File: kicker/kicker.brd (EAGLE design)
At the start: 59.7 x 56.3 mm, 26 parts, among them T1 NPN_BC817,215, T3 NPN_BC817,215, X1 JST-XH-06-PIN-LONG-PAD

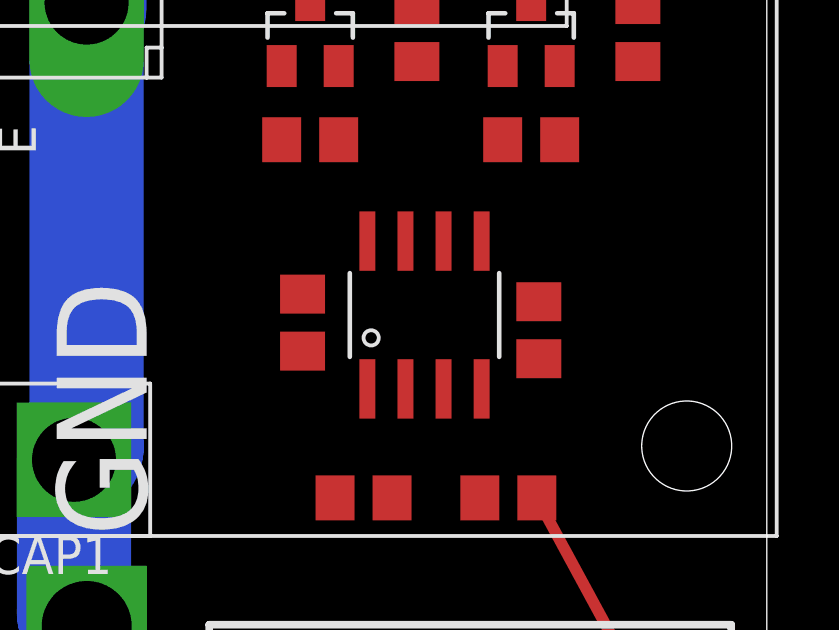
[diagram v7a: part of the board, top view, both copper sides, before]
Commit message: Adding optional npn for kicking
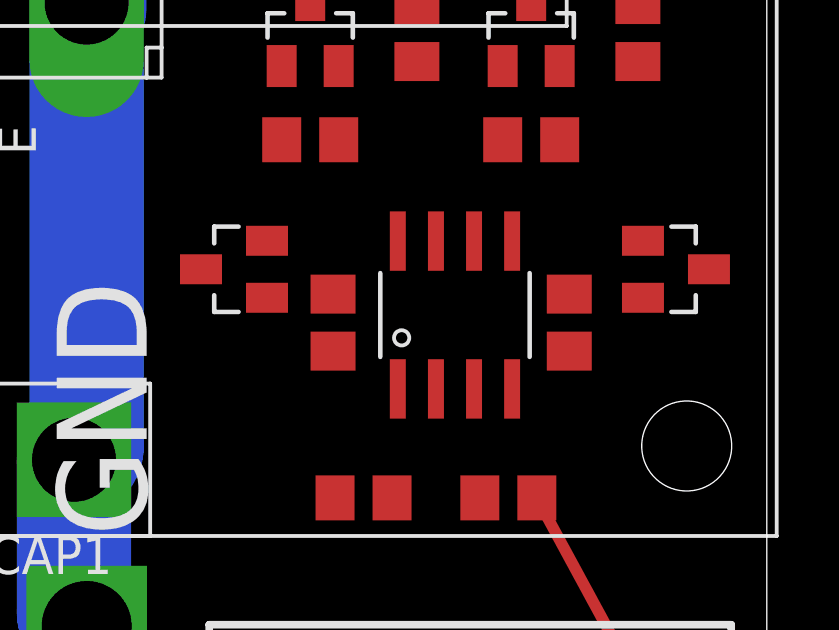
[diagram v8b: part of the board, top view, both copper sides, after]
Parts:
- added T2, T4: NPN_BC817,215, rhoban:SOT-23
- moved R8 1.05 mm to (53.1, 14.7)
- moved R7 1.02 mm to (45.2, 14.7)
- moved U$4 1.02 mm to (49.3, 15.0)
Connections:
- removed net N$10: R8.1, U$4.3
- removed net N$9: R7.1, U$4.1
- new net KICK1R: R7.1, T2.1, U$4.1
- new net KICK2R: R8.1, T4.1, U$4.3
- net GND: now also T2.2, T4.2
- net KICK_TR1: now also T2.3
- net KICK_TR2: now also T4.3
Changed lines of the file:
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@@
 <param name="mtCopper" value="0.035mm 0.035mm 0.035mm 0.035mm 0.035mm 0.035mm 0.035mm 0.035mm 0.035mm 0.035mm 0.035mm 0.035mm 0.035mm 0.035mm 0.035mm 0.035mm"/>
 <param name="mtIsolate" value="1.5mm 0.15mm 0.2mm 0.15mm 0.2mm 0.15mm 0.2mm 0.15mm 0.2mm 0.15mm 0.2mm 0.15mm 0.2mm 0.15mm 0.2mm"/>
-<param name="mdWireWire" value="10mil"/>
+<param name="mdWireWire" value="15mil"/>
 <param name="mdWirePad" value="20mil"/>
 <param name="mdWireVia" value="20mil"/>
@@
 <attribute name="FARNELL" value="2446965" x="51.816" y="28.702" size="1.778" layer="27" rot="R270" display="off"/>
 </element>
-<element name="U$4" library="rhoban" package="SO8" value="ACPL-227-500E" x="48.26" y="14.986" rot="R90">
-<attribute name="FARNELL" value="1634749RL" x="48.26" y="14.986" size="1.778" layer="27" rot="R90" display="off"/>
-</element>
-<element name="R7" library="rhoban" package="R0805" value="3K" x="44.196" y="14.732" rot="R90">
-<attribute name="FARNELL" value="2446965" x="44.196" y="14.732" size="1.778" layer="27" rot="R90" display="off"/>
-</element>
-<element name="R8" library="rhoban" package="R0805" value="3K" x="52.07" y="14.478" rot="R90">
-<attribute name="FARNELL" value="2446965" x="52.07" y="14.478" size="1.778" layer="27" rot="R90" display="off"/>
+<element name="U$4" library="rhoban" package="SO8" value="ACPL-227-500E" x="49.276" y="14.986" rot="R90">
+<attribute name="FARNELL" value="1634749RL" x="49.276" y="14.986" size="1.778" layer="27" rot="R90" display="off"/>
+</element>
+<element name="R7" library="rhoban" package="R0805" value="3K" x="45.212" y="14.732" rot="R90">
+<attribute name="FARNELL" value="2446965" x="45.212" y="14.732" size="1.778" layer="27" rot="R90" display="off"/>
+</element>
+<element name="R8" library="rhoban" package="R0805" value="3K" x="53.086" y="14.732" rot="R90">
+<attribute name="FARNELL" value="2446965" x="53.086" y="14.732" size="1.778" layer="27" rot="R90" display="off"/>
+</element>
+<element name="T2" library="rhoban" package="SOT-23" value="NPN_BC817,215" x="41.91" y="16.51" rot="R90">
+<attribute name="FARNELL" value="1081223" x="41.91" y="16.51" size="1.778" layer="27" rot="R90" display="off"/>
+</element>
+<element name="T4" library="rhoban" package="SOT-23" value="NPN_BC817,215" x="56.642" y="16.51" rot="R270">
+<attribute name="FARNELL" value="1081223" x="57.15" y="16.51" size="1.778" layer="27" rot="R270" display="off"/>
 </element>
 </elements>
@@
 <contactref element="X1" pad="5"/>
 <contactref element="R8" pad="2"/>
-<wire x1="52.07" y1="15.428" x2="53.594" y2="1.27" width="0" layer="19" extent="1-1"/>
+<wire x1="53.594" y1="1.27" x2="53.086" y2="15.682" width="0" layer="19" extent="1-1"/>
 </signal>
 <signal name="GND" class="2">
@@
 <contactref element="U$4" pad="7"/>
 <contactref element="U$4" pad="5"/>
-<wire x1="50.165" y1="17.4498" x2="52.766" y2="23.284" width="0" layer="19" extent="1-1"/>
-<wire x1="47.625" y1="17.4498" x2="50.165" y2="17.4498" width="0" layer="19" extent="1-1"/>
-<wire x1="50.165" y1="12.5222" x2="50.165" y2="17.4498" width="0" layer="19" extent="1-1"/>
-<wire x1="47.625" y1="12.5222" x2="50.165" y2="12.5222" width="0" layer="19" extent="1-1"/>
-<wire x1="50.104" y1="8.89" x2="50.165" y2="12.5222" width="0" layer="19" extent="1-1"/>
-<wire x1="45.4" y1="23.284" x2="47.625" y2="17.4498" width="0" layer="19" extent="1-1"/>
-<wire x1="36.996" y1="25.4" x2="45.4" y2="23.284" width="0" layer="19" extent="1-1"/>
+<wire x1="32.766" y1="32.766" x2="37.084" y2="28.448" width="3.81" layer="16" curve="-90"/>
+<wire x1="37.084" y1="28.448" x2="37.084" y2="25.146" width="3.81" layer="16"/>
+<contactref element="T2" pad="2"/>
+<contactref element="T4" pad="2"/>
+<wire x1="51.181" y1="17.4498" x2="52.766" y2="23.284" width="0" layer="19" extent="1-1"/>
+<wire x1="48.641" y1="17.4498" x2="51.181" y2="17.4498" width="0" layer="19" extent="1-1"/>
+<wire x1="55.542" y1="15.56" x2="51.181" y2="17.4498" width="0" layer="19" extent="1-1"/>
+<wire x1="51.181" y1="12.5222" x2="51.181" y2="17.4498" width="0" layer="19" extent="1-1"/>
+<wire x1="48.641" y1="12.5222" x2="51.181" y2="12.5222" width="0" layer="19" extent="1-1"/>
+<wire x1="50.104" y1="8.89" x2="51.181" y2="12.5222" width="0" layer="19" extent="1-1"/>
+<wire x1="43.01" y1="17.46" x2="48.641" y2="12.5222" width="0" layer="19" extent="1-1"/>
+<wire x1="45.4" y1="23.284" x2="48.641" y2="17.4498" width="0" layer="19" extent="1-1"/>
+<wire x1="36.996" y1="10.58" x2="43.01" y2="17.46" width="0" layer="19" extent="1-16"/>
+<wire x1="37.084" y1="25.146" x2="36.996" y2="25.4" width="0" layer="19" extent="16-16"/>
 <wire x1="43.434" y1="1.27" x2="37" y2="0.17" width="0" layer="19" extent="16-16"/>
 <wire x1="8.72" y1="14.92" x2="19.47" y2="25.4" width="0" layer="19" extent="1-1"/>
 <wire x1="11" y1="4.62" x2="8.72" y2="14.92" width="0" layer="19" extent="1-1"/>
-<wire x1="32.766" y1="32.766" x2="37.084" y2="28.448" width="3.81" layer="16" curve="-90"/>
-<wire x1="37.084" y1="28.448" x2="37.084" y2="25.146" width="3.81" layer="16"/>
-<wire x1="37.084" y1="25.146" x2="36.996" y2="25.4" width="0" layer="19" extent="1-16"/>
 </signal>
 <signal name="N$4">
@@
 <contactref element="X1" pad="4"/>
 <contactref element="R7" pad="2"/>
-<wire x1="44.196" y1="15.682" x2="51.054" y2="1.27" width="0" layer="19" extent="1-1"/>
+<wire x1="51.054" y1="1.27" x2="45.212" y2="15.682" width="0" layer="19" extent="1-1"/>
 </signal>
 <signal name="CAP">
@@
 <contactref element="T1" pad="1"/>
 <contactref element="U$4" pad="8"/>
+<contactref element="T2" pad="3"/>
 <wire x1="43.5" y1="20.828" x2="43.5" y2="23.284" width="0" layer="19" extent="1-1"/>
-<wire x1="46.355" y1="17.4498" x2="43.5" y2="20.828" width="0" layer="19" extent="1-1"/>
+<wire x1="40.81" y1="16.51" x2="43.5" y2="20.828" width="0" layer="19" extent="1-1"/>
+<wire x1="47.371" y1="17.4498" x2="43.5" y2="20.828" width="0" layer="19" extent="1-1"/>
 </signal>
 <signal name="KICK_TR2">
@@
 <contactref element="T3" pad="1"/>
 <contactref element="U$4" pad="6"/>
+<contactref element="T4" pad="3"/>
 <wire x1="50.866" y1="20.828" x2="50.866" y2="23.284" width="0" layer="19" extent="1-1"/>
-<wire x1="48.895" y1="17.4498" x2="50.866" y2="20.828" width="0" layer="19" extent="1-1"/>
+<wire x1="49.911" y1="17.4498" x2="50.866" y2="20.828" width="0" layer="19" extent="1-1"/>
+<wire x1="57.742" y1="16.51" x2="49.911" y2="17.4498" width="0" layer="19" extent="1-1"/>
 </signal>
 <signal name="N$7">
@@
 <wire x1="8.47" y1="25.4" x2="51.816" y2="29.652" width="0" layer="19" extent="1-1"/>
 </signal>
-<signal name="N$9">
+<signal name="KICK1R">
 <contactref element="U$4" pad="1"/>
 <contactref element="R7" pad="1"/>
-<wire x1="46.355" y1="12.5222" x2="44.196" y2="13.782" width="0" layer="19" extent="1-1"/>
-</signal>
-<signal name="N$10">
+<contactref element="T2" pad="1"/>
+<wire x1="45.212" y1="13.782" x2="47.371" y2="12.5222" width="0" layer="19" extent="1-1"/>
+<wire x1="43.01" y1="15.56" x2="45.212" y2="13.782" width="0" layer="19" extent="1-1"/>
+</signal>
+<signal name="KICK2R">
 <contactref element="U$4" pad="3"/>
 <contactref element="R8" pad="1"/>
-<wire x1="48.895" y1="12.5222" x2="52.07" y2="13.528" width="0" layer="19" extent="1-1"/>
+<contactref element="T4" pad="1"/>
+<wire x1="53.086" y1="13.782" x2="55.542" y2="17.46" width="0" layer="19" extent="1-1"/>
+<wire x1="49.911" y1="12.5222" x2="53.086" y2="13.782" width="0" layer="19" extent="1-1"/>
 </signal>
 </signals>
